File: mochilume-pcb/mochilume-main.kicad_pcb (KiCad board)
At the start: 2 copper layers, 90 x 60.1 mm, 28 parts, among them U1 llcc68_custom_module

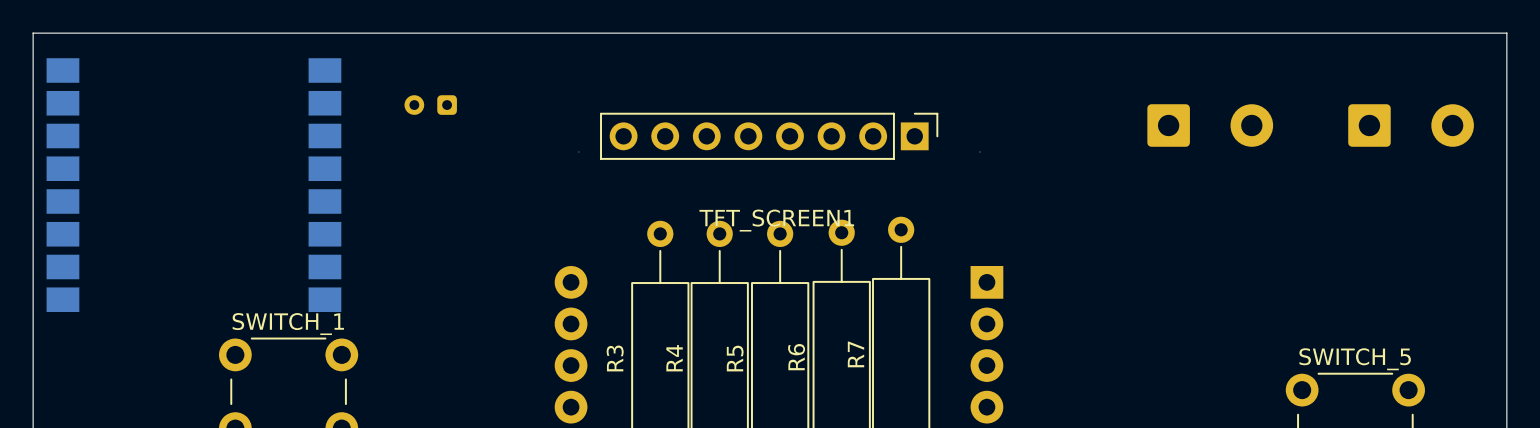
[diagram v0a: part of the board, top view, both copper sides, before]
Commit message: refactor pcb: split power and logic into 2 pcbs
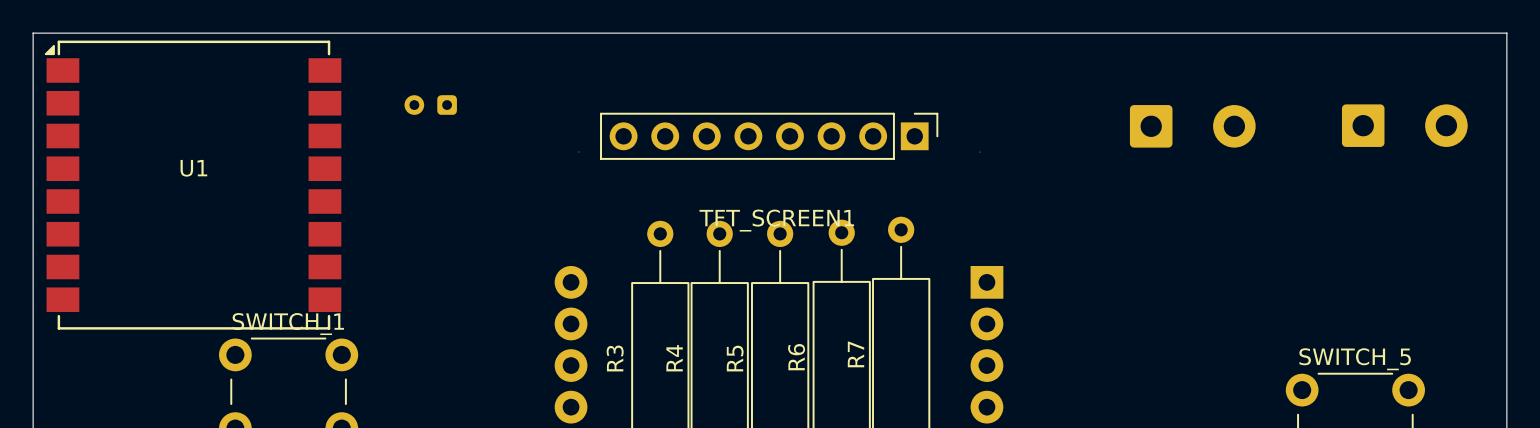
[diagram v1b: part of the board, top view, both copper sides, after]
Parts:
- U1: moved to F.Cu
- moved ON/OFF1 1.07 mm to (241.3, 88.4)
- moved BATTERRY_BORN1 0.38 mm to (254.2, 88.3)
- turned U1 to 0 degrees

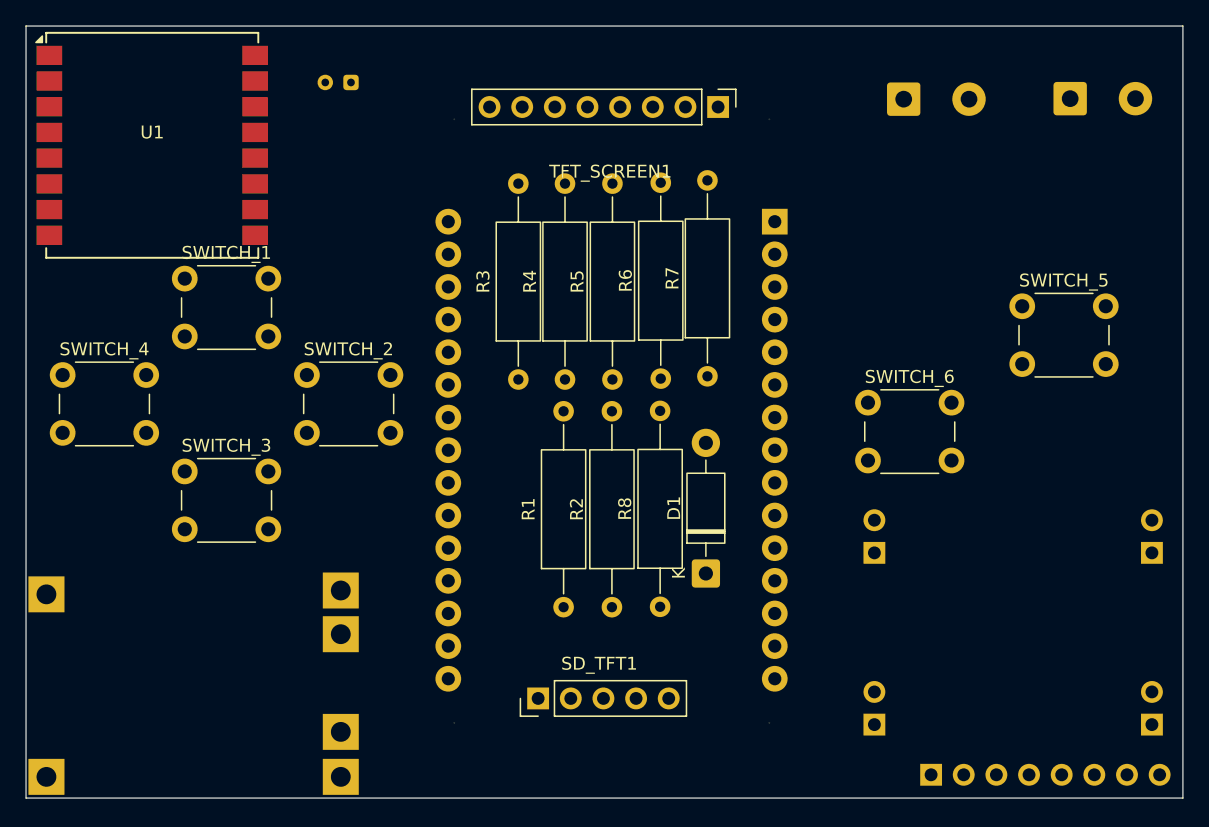
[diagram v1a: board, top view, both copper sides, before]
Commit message: feat main pcb: add vias tracking to main pcb
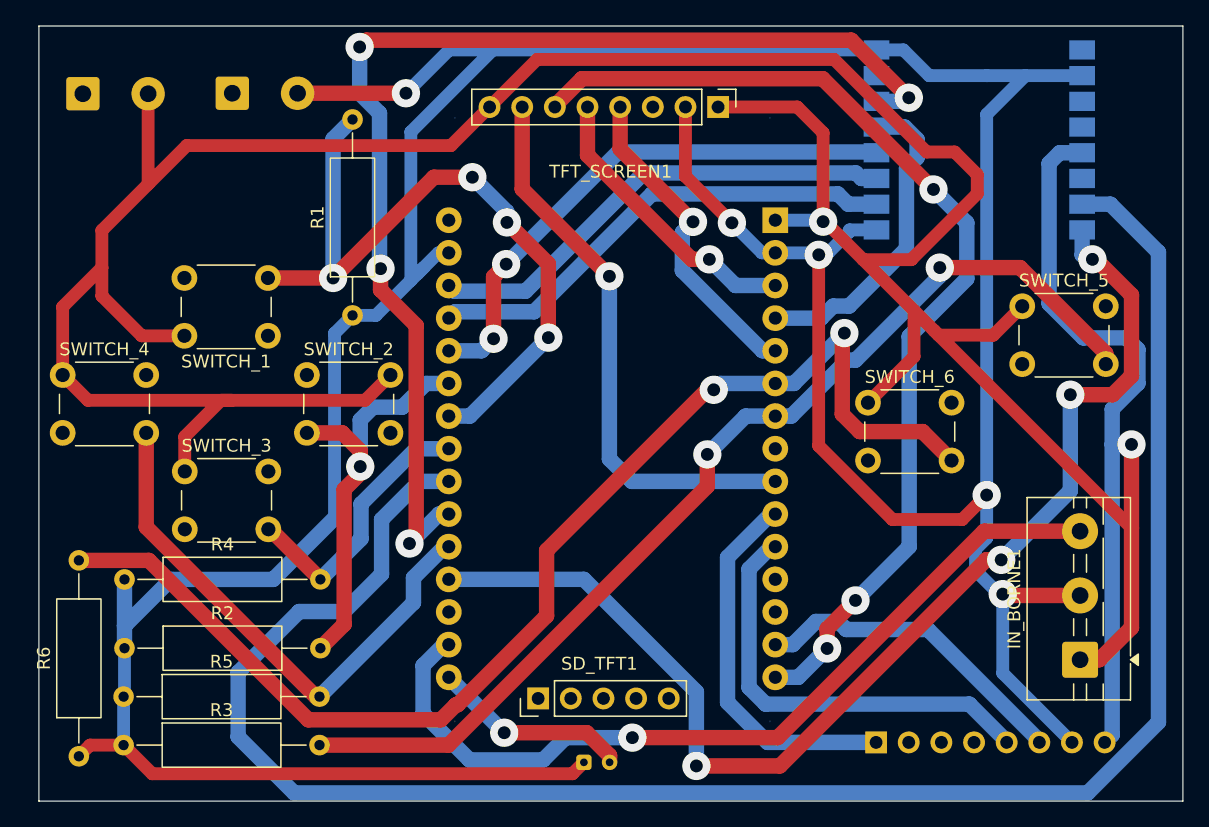
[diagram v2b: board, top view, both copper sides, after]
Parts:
- removed D1: 1N5819, Diode_THT:D_DO-41_SOD81_P10.16mm_Horizontal
- removed GND1, GNDIN1, VIN1, VOUT1: ~, Connector_PinHeader_2.54mm:PinHeader_1x02_P2.54mm_Vertical
- removed R7, R8: 10K, Resistor_THT:R_Axial_DIN0309_L9.0mm_D3.2mm_P15.24mm_Horizontal
- removed TP1: ~, Library:TP4056-18650
- added IN_BORNE1: Screw_Terminal_01x03, TerminalBlock:TerminalBlock_MaiXu_MX126-5.0-03P_1x03_P5.00mm, F.Cu at (255.0, 132.0)
- U1: moved to B.Cu
- moved BATTERRY_BORN1 65.2 mm to (189.0, 87.9)
- moved U1 64.3 mm to (247.2, 91.6), turned to 180 degrees
- moved ON/OFF1 63.9 mm to (177.4, 88.0)
- moved C1 55.9 mm to (216.4, 140.0), turned to 0 degrees
- moved R6 54.0 mm to (177.1, 139.5)
- moved R5 45.3 mm to (180.6, 134.9), turned to 0 degrees
- moved R3 41.9 mm to (180.6, 138.6), turned to 0 degrees
- moved R2 38.1 mm to (180.7, 131.1), turned to 0 degrees
- moved R4 37.6 mm to (180.7, 125.8), turned to 0 degrees
- moved R1 28.0 mm to (198.4, 105.2)
- moved SWITCH_1 7.85 mm to (191.8, 106.8), turned to 180 degrees
- moved ACCELEROMETER1 4.97 mm to (239.1, 138.4)
- moved ESP32-WROOM-DEVKIT-V1 0.12 mm to (218.6, 113.3)
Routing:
- net GND: track 0.00 -> 301.7 mm, vias 0 -> 5
- net VCC: track 0.00 -> 299.4 mm, vias 0 -> 2
- net LORA_DIO1: track 0.00 -> 149.8 mm
- net SW_6: track 0.00 -> 96.5 mm, vias 0 -> 2
- net LORA_BUSY: track 0.00 -> 92.8 mm, vias 0 -> 4
- net LORA_RST: track 0.00 -> 92.1 mm, vias 0 -> 4
- net SW_5: track 0.00 -> 82.0 mm, vias 0 -> 2
- net TFT_SDA: track 0.00 -> 80.2 mm, vias 0 -> 3
- net BATERIA: track 0.00 -> 66.4 mm, vias 0 -> 1
- net SW_1: track 0.00 -> 57.3 mm, vias 0 -> 4
- net TFT_SCK: track 0.00 -> 43.8 mm, vias 0 -> 1
- net LORA_SCK: track 0.00 -> 42.5 mm, vias 0 -> 2
- net SW_4: track 0.00 -> 42.3 mm
- net LORA_MISO: track 0.00 -> 37.6 mm
- net LORA_MOSI: track 0.00 -> 37.4 mm
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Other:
- board size 90 x 60.1 mm -> 89 x 60.3 mm

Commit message: fix: unconnected via between tft_cs and esp 32 pin 8
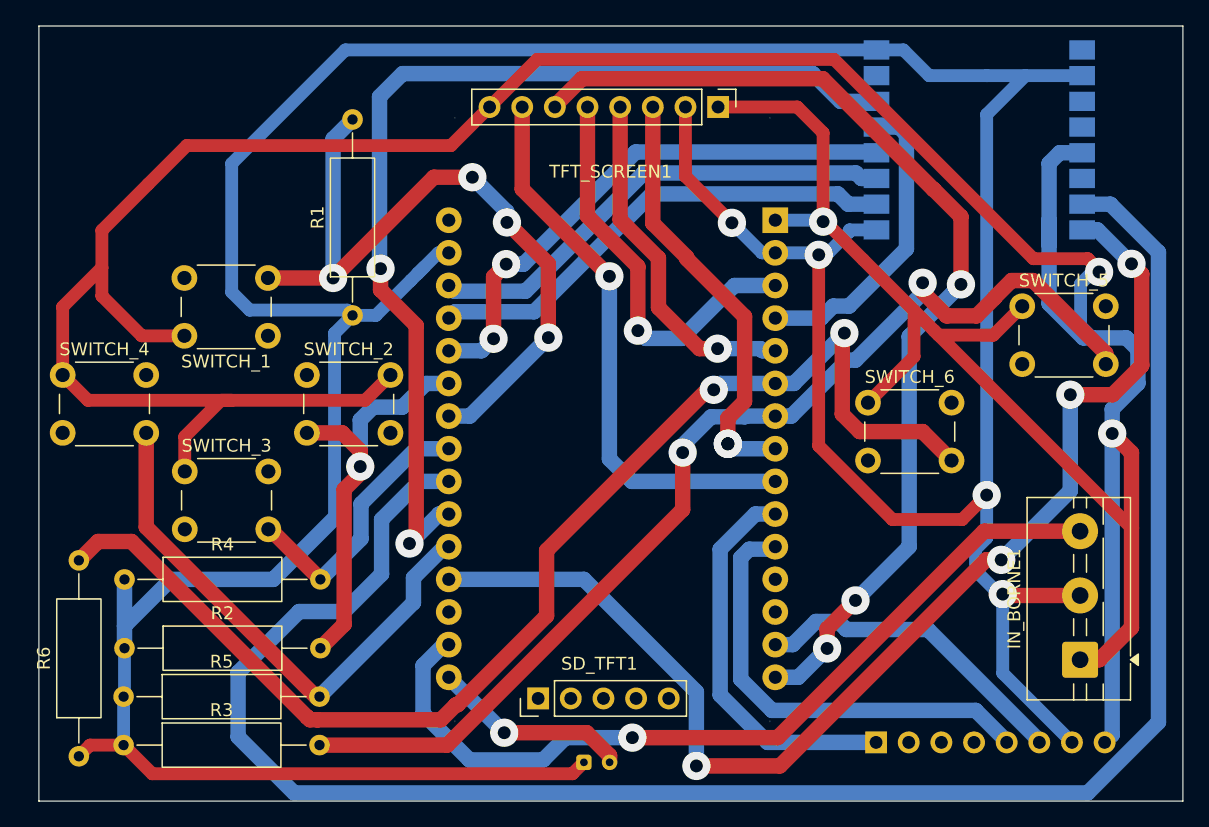
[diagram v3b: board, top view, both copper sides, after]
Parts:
- removed BATTERRY_BORN1, ON/OFF1: ~, TerminalBlock_Phoenix:TerminalBlock_Phoenix_MKDS-1,5-2-5.08_1x02_P5.08mm_Horizontal
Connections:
- ESP32-WROOM-DEVKIT-V1 pad 8: unconnected-(ESP32-WROOM-DEVKIT-V1-D5-Pad8) -> TFT_CS
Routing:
- net TFT_CS: track 0.00 -> 33.5 mm, vias 0 -> 2
- net LORA_RST: track 92.1 -> 80.5 mm, vias 4 -> 2
- net TFT_A0: track 22.6 -> 31.7 mm
- net GND: track 301.7 -> 308.7 mm, vias 5 -> 4
- net SW_5: track 82.0 -> 85.6 mm
- net TFT_RES: track 25.2 -> 27.3 mm
- net VCC: track 299.4 -> 301.1 mm, vias 2 -> 3
- net AC_SDA: track 33.8 -> 35.3 mm
- net SW_6: track 96.5 -> 97.7 mm
- net AC_TRIG: track 29.2 -> 30.4 mm
- net LORA_CS: track 24.8 -> 23.9 mm
- net LORA_BUSY: track 92.8 -> 93.8 mm
